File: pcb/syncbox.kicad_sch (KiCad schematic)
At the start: 100 parts, among them J1 DC 7-12V, J2 SWD, J3 USB_B, J4 IN, J5 SYNC1, J6 SYNC2, J7 Gate 1, J8 Gate 2, J9 Gate 3, Q1 PMBT2907A, Q2 PMBT2907A, Q3 PMBT2907A, Q4 PMBT2907A, Q5 PMBT2907A, Q6 PMBT2907A, Q7 PMBT2907A, Q8 PMBT2907A, Q9 PMBT2907A, U1 LD1117S50TR_SOT223, U2 STM32F303RET6, U3 ADP150, U4 RV1S9160A, U5 CD74HCT04, X1 ECS-TXO-2520 24MHz

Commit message: Version 1.1 hardware changes
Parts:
- removed TP1: E5V, Syncbox:TestPoint_Pad_D1.5mm, symbol Connector:TestPoint
- removed TP6: U5V, Syncbox:TestPoint_Pad_D1.5mm, symbol Connector:TestPoint
- added Q10: MMBT2222A, Package_TO_SOT_SMD:SOT-23_Handsoldering, symbol Transistor_BJT:MMBT3904
- added R33: 10k, Resistor_SMD:R_0805_2012Metric_Pad1.20x1.40mm_HandSolder, symbol Device:R
- added R34: 100, Resistor_SMD:R_0805_2012Metric_Pad1.20x1.40mm_HandSolder, symbol Device:R
- added R35: 36k, Resistor_SMD:R_0805_2012Metric_Pad1.20x1.40mm_HandSolder, symbol Device:R
- D2, D6, D7: value BAT42 -> BAT60J; footprint Syncbox:D_0805_2012Metric_Pad1.15x1.40mm_HandSolder -> Diode_SMD:D_SOD-323_HandSoldering
- D3, D4, D5: value TVS -> TVS PGB1010603
- JP1: value DFU -> B0
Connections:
- net +3V3: now also Q10.3 (C); no longer R2.2
- net GND: now also R35.2
- net USBD_P: now also R2.2; no longer R2.1
- net SENSE: now reaches U2.42 (PA9)
- net SENSE: now also R34.2
- net U5V: now reaches C10.1, C11.1, D6.2 (A), FB3.1
- net U5V: now also R33.1
- net E5V: now reaches C2.1, D2.2 (A), U1.2 (VO)
- new net: Q10.2 (E), R2.1
- new net: Q10.1 (B), R33.2, R34.1, R35.1
- no-connect marks 45 -> 44
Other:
- moved on the sheet: B1, D6, R2

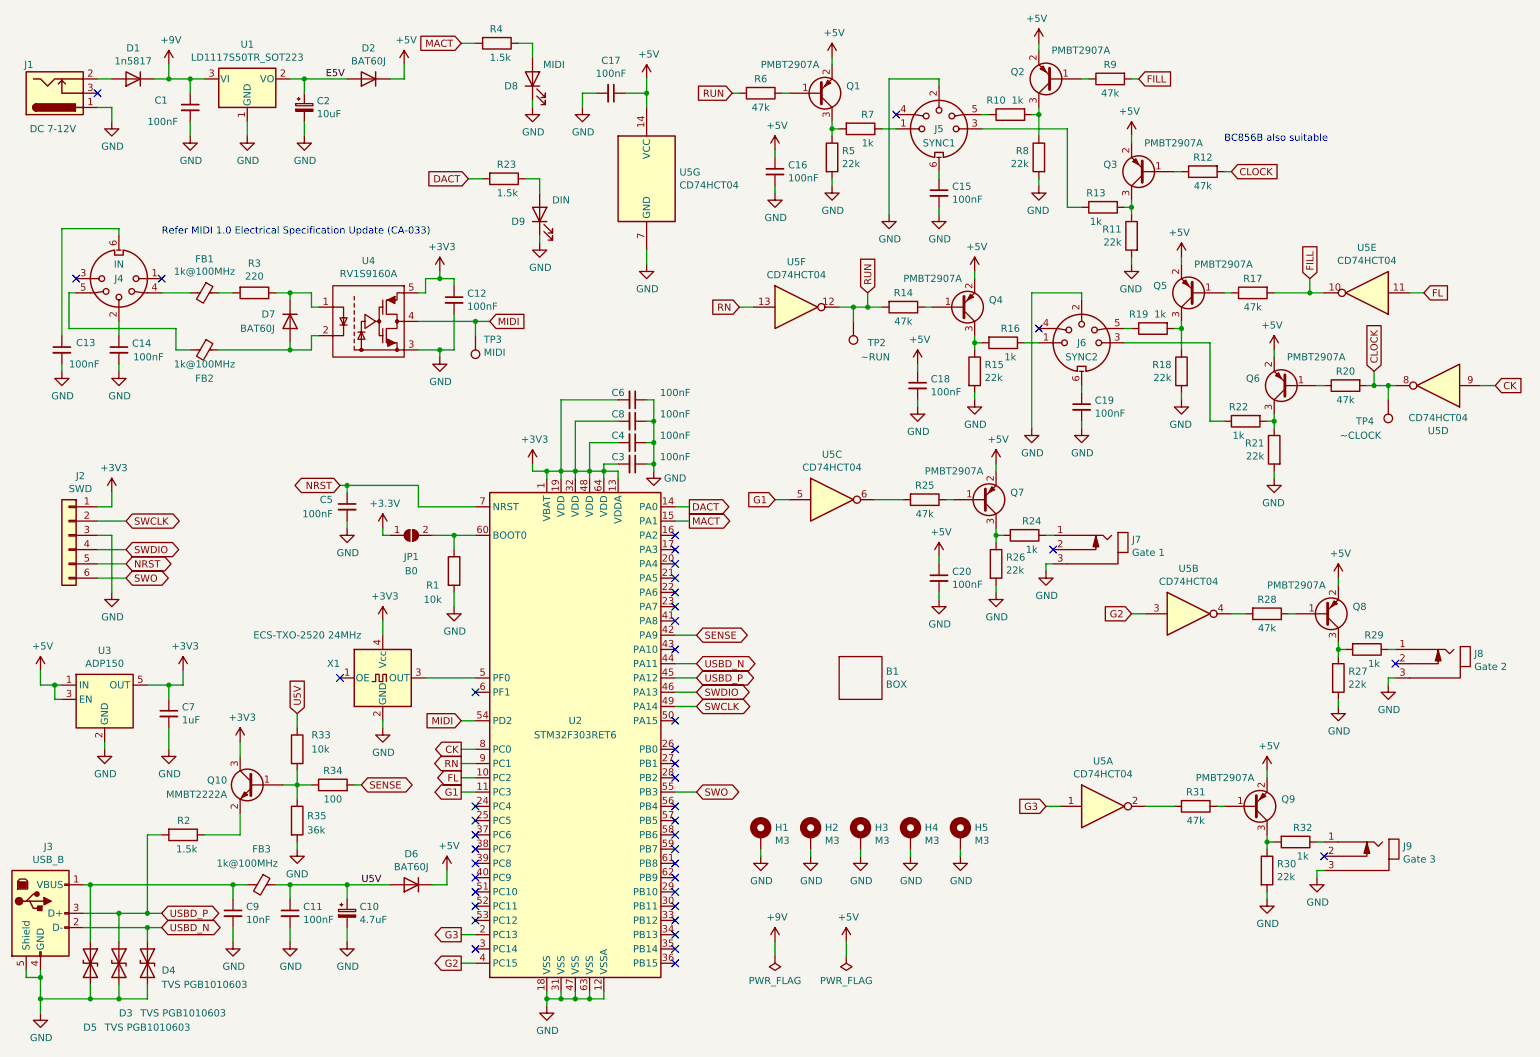
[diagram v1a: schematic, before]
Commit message: Update schematic and top label
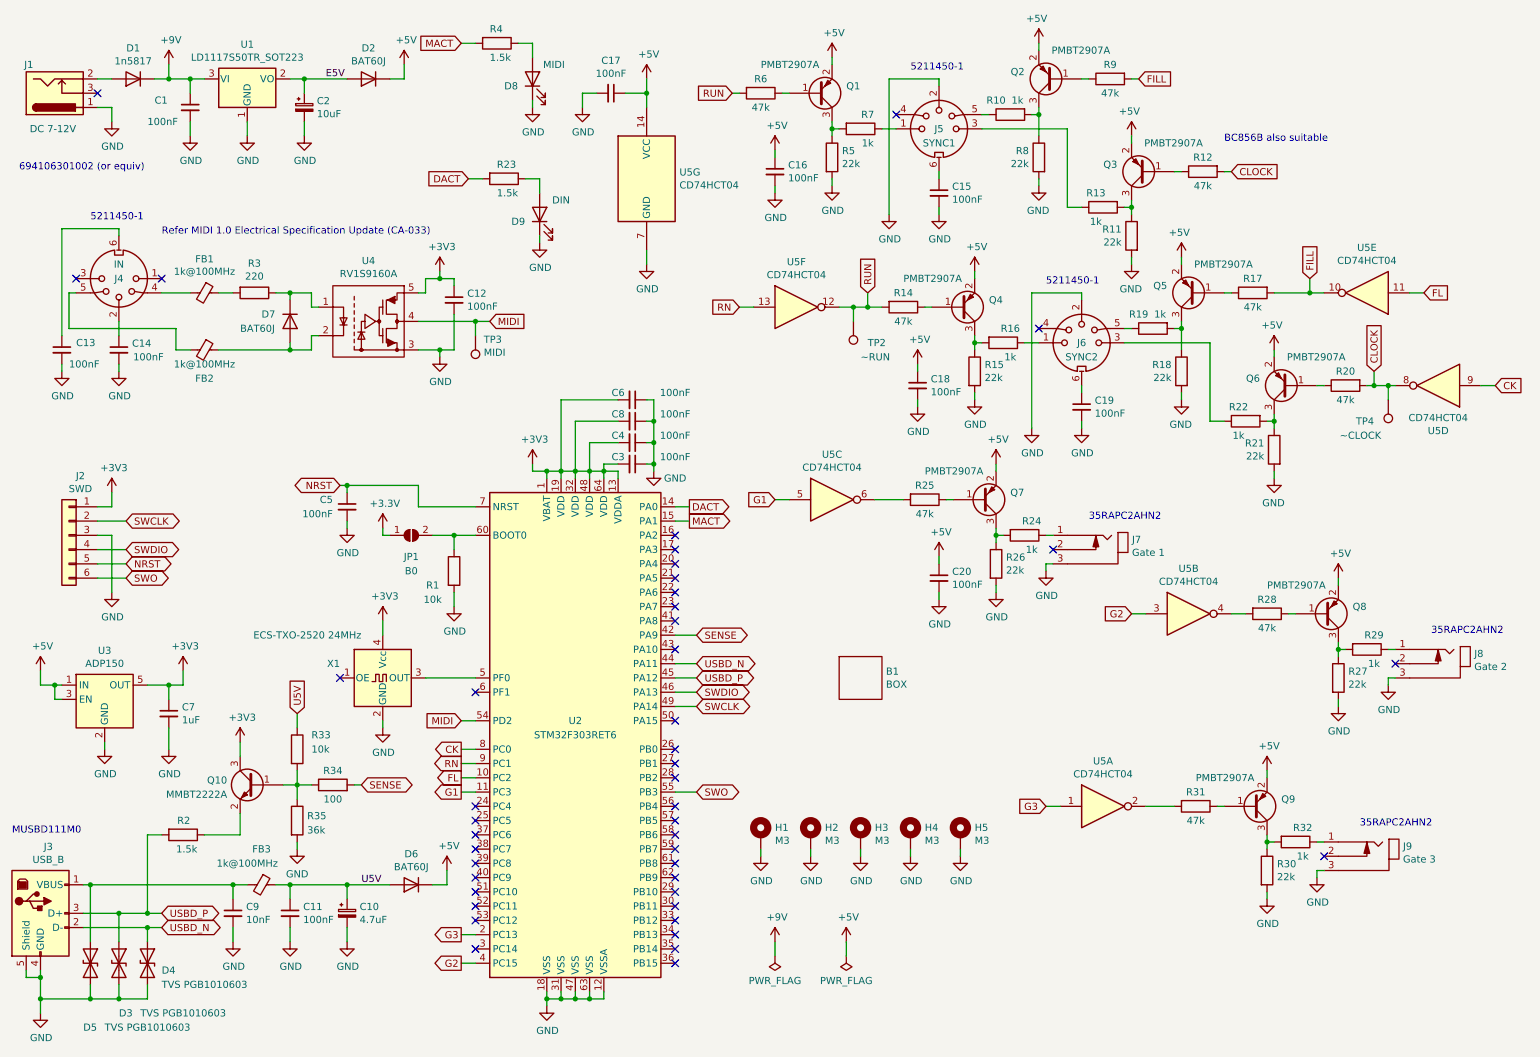
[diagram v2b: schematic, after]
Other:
- note added: "35RAPC2AHN2"
- note added: "5211450-1"
- note added: "694106301002 (or equiv)"
- note added: "MUSBD111M0"
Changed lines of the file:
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@@
     (stroke (width 0) (type default) (color 0 0 0 0))
+  )
+  (text "5211450-1" (at 29.21 50.8 0)
+    (effects (font (size 1.27 1.27)) (justify left bottom))
   )
   (text "Refer MIDI 1.0 Electrical Specification Update (CA-033)"
@@
     (effects (font (size 1.27 1.27)) (justify left bottom))
   )
+  (text "5211450-1" (at 199.39 62.23 0)
+    (effects (font (size 1.27 1.27)) (justify left bottom))
+  )
+  (text "35RAPC2AHN2" (at 207.01 104.14 0)
+    (effects (font (size 1.27 1.27)) (justify left bottom))
+  )
   (text "BC856B also suitable" (at 231.14 36.83 0)
     (effects (font (size 1.27 1.27)) (justify left bottom))
   )
+  (text "694106301002 (or equiv)" (at 16.51 41.91 0)
+    (effects (font (size 1.27 1.27)) (justify left bottom))
+  )
+  (text "35RAPC2AHN2" (at 255.27 158.75 0)
+    (effects (font (size 1.27 1.27)) (justify left bottom))
+  )
+  (text "MUSBD111M0" (at 15.24 160.02 0)
+    (effects (font (size 1.27 1.27)) (justify left bottom))
+  )
+  (text "5211450-1" (at 175.26 24.13 0)
+    (effects (font (size 1.27 1.27)) (justify left bottom))
+  )
+  (text "35RAPC2AHN2" (at 267.97 124.46 0)
+    (effects (font (size 1.27 1.27)) (justify left bottom))
+  )
